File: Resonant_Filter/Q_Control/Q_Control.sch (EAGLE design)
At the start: 23 parts, among them T1 2SC3324, U1 OPA209

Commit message: Licenses
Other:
- note added: "Q Control Project by Cycfi Research is licensed under a Creative Commons Attribution-ShareAlike 4.0 International License. Copyright CYCFI Research Inc. 2013-2016"
- note removed: "Resonant Filter Project by Cycfi Research is licensed under a Creative Commons Attribution-NonCommercial 4.0 International License. http://creativecommons.org/licenses/by-nc/4.0/ Copyright CYCFI Research Inc. 2013-2016"
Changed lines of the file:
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@@
 <text x="177.8" y="19.05" size="2.54" layer="95">Q Control</text>
 <text x="253.365" y="6.985" size="2.1844" layer="95">v1.46</text>
-<text x="7.62" y="12.7" size="2.54" layer="95">Resonant Filter Project by Cycfi Research is licensed under a
-Creative Commons Attribution-NonCommercial 4.0 International License.
-http://creativecommons.org/licenses/by-nc/4.0/
+<text x="7.62" y="12.7" size="2.54" layer="95">Q Control Project by Cycfi Research is licensed under a
+Creative Commons Attribution-ShareAlike 4.0 International License.
 Copyright CYCFI Research Inc. 2013-2016</text>
 <text x="200.66" y="11.43" size="2.54" layer="95">2016041</text>

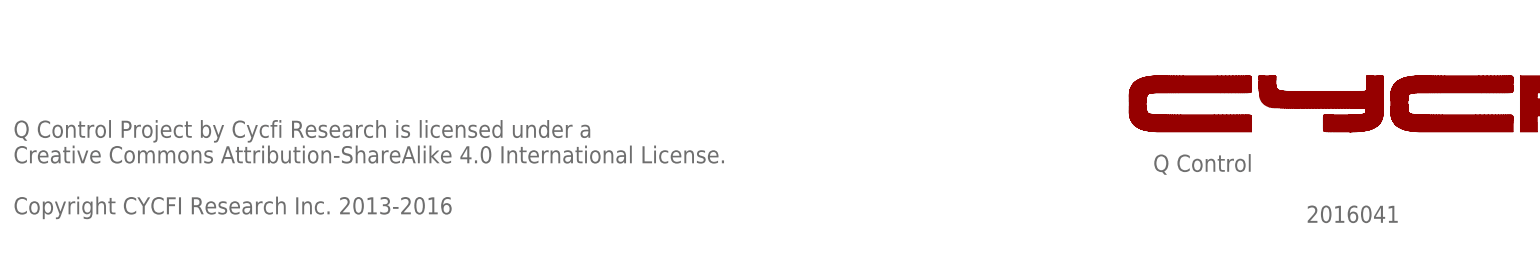
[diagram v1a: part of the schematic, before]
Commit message: *organize 5-waay switch and its configuration board(a and b) *update license date *remove red frame schem pdf files, change with black frame *update document number
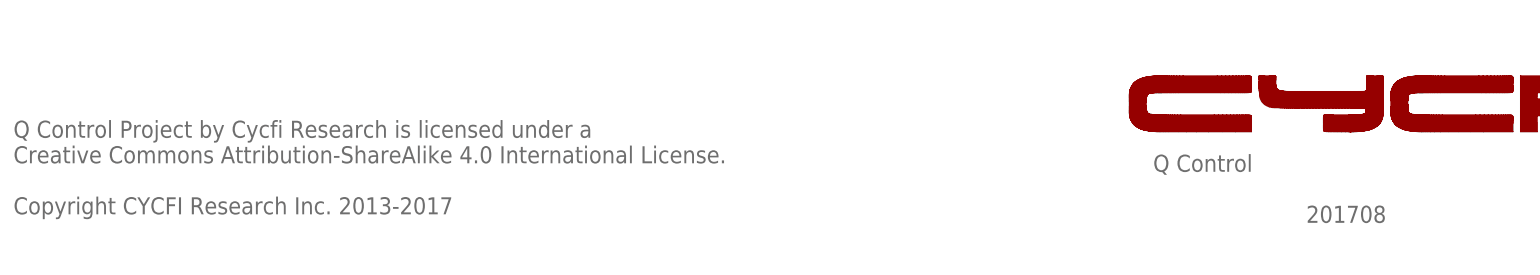
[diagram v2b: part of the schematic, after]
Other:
- note added: "201708"
- note added: "Q Control Project by Cycfi Research is licensed under a Creative Commons Attribution-ShareAlike 4.0 International License. Copyright CYCFI Research Inc. 2013-2017"
- note removed: "2016041"
- note removed: "Q Control Project by Cycfi Research is licensed under a Creative Commons Attribution-ShareAlike 4.0 International License. Copyright CYCFI Research Inc. 2013-2016"
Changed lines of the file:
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@@
 <text x="7.62" y="12.7" size="2.54" layer="95">Q Control Project by Cycfi Research is licensed under a
 Creative Commons Attribution-ShareAlike 4.0 International License.
-Copyright CYCFI Research Inc. 2013-2016</text>
-<text x="200.66" y="11.43" size="2.54" layer="95">2016041</text>
+Copyright CYCFI Research Inc. 2013-2017</text>
+<text x="200.66" y="11.43" size="2.54" layer="95">201708</text>
 <wire x1="192.47528125" y1="25.047221875" x2="190.115640625" y2="25.047221875" width="0" layer="94"/>
 <wire x1="190.115640625" y1="25.047221875" x2="188.10833125" y2="25.047225" width="0" layer="94"/>

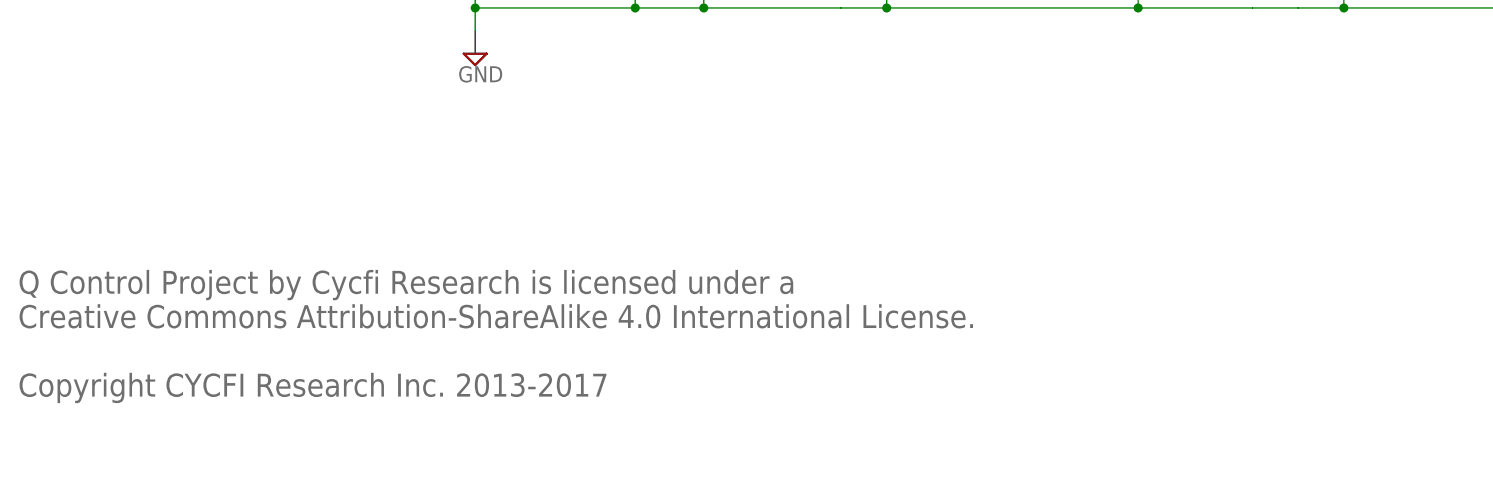
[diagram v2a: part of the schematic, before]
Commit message: Updated broken .sch files
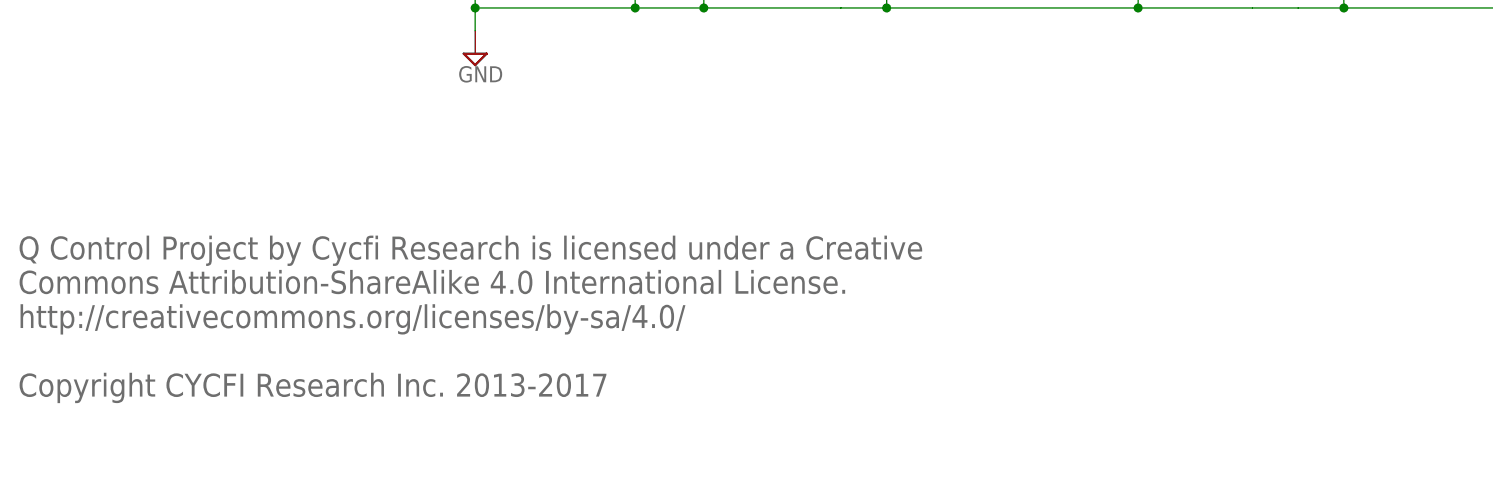
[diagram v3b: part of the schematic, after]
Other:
- note added: "Q Control Project by Cycfi Research is licensed under a Creative Commons Attribution-ShareAlike 4.0 International License. http://creativecommons.org/licenses/by-sa/4.0/ Copyright CYCFI Research Inc. 2013-2017"
- note removed: "Q Control Project by Cycfi Research is licensed under a Creative Commons Attribution-ShareAlike 4.0 International License. Copyright CYCFI Research Inc. 2013-2017"
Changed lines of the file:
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@@
 <text x="177.8" y="19.05" size="2.54" layer="95">Q Control</text>
 <text x="253.365" y="6.985" size="2.1844" layer="95">v1.46</text>
-<text x="7.62" y="12.7" size="2.54" layer="95">Q Control Project by Cycfi Research is licensed under a
-Creative Commons Attribution-ShareAlike 4.0 International License.
+<text x="7.62" y="12.7" size="2.54" layer="95">Q Control Project by Cycfi Research is licensed under a Creative
+Commons Attribution-ShareAlike 4.0 International License.
+http://creativecommons.org/licenses/by-sa/4.0/
 Copyright CYCFI Research Inc. 2013-2017</text>
 <text x="200.66" y="11.43" size="2.54" layer="95">201708</text>
